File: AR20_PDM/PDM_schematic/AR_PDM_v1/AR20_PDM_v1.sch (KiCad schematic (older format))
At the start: 21 parts, among them J1 S_T_?, J2 1-776163-1, U1 ACM_2020

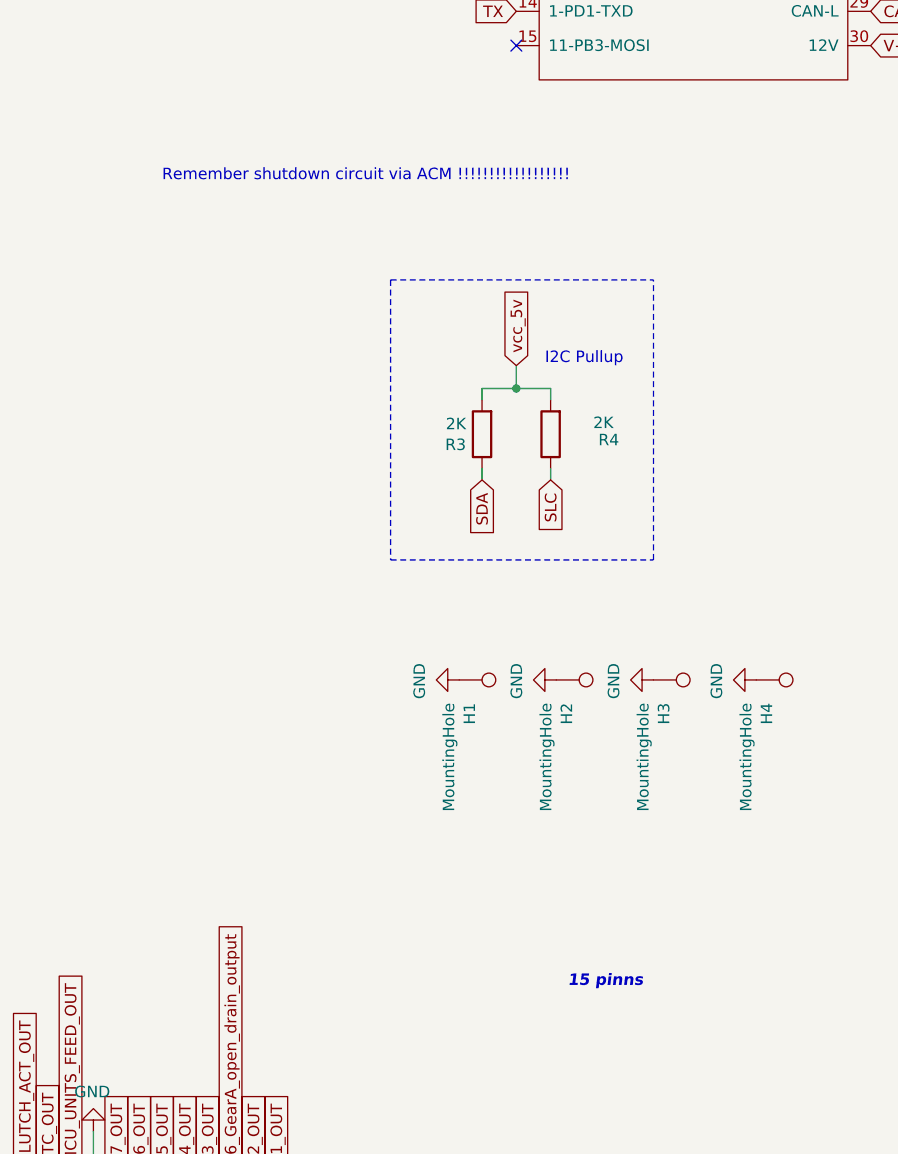
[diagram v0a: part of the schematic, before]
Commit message: Generated new gerberfile, with forgotten solder mask
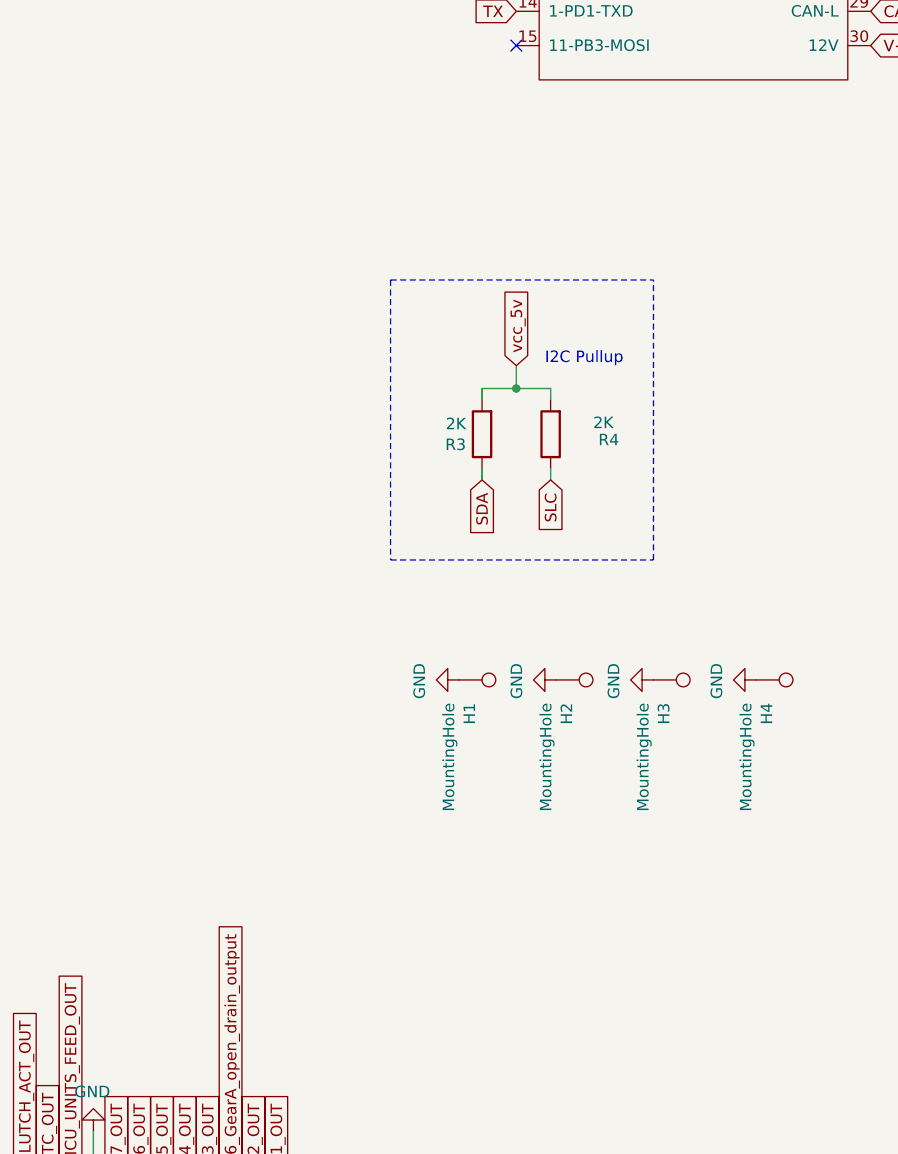
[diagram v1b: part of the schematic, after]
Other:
- note removed: "15 pinns"
- note removed: "Remember shutdown circuit via ACM !!!!!!!!!!!!!!!!!!"
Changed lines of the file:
@@
 Text GLabel 8775 7875 1    50   Input ~ 0
 SHUTDOWN_OUT
-Text Notes 13850 7050 0    50   Italic 10
-15 pinns
 Text Notes 13750 4325 0    50   ~ 0
 I2C Pullup
@@
 Wire Wire Line
 	2125 4475 2225 4475
-Text Notes 12075 3525 0    50   ~ 0
-Remember shutdown circuit via ACM !!!!!!!!!!!!!!!!!!
 Text GLabel 10100 1275 2    50   Input ~ 0
 ACM_Shutdown_Circuit

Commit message: Major redesign. schematics completed, PCB work in progress
-TODO : A proper changelog file. Where all changes will apear 
- Redesigned schematics to accommodate errors in the improvement list
- More detail in ALPHA improvement list
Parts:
- D1, D2, D3, D4: symbol AR20_PDM_v1-rescue:D_Zener-Device -> AR20_PDM_v1-rescue:D_Flyback-Zener
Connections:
- net labels added: Mux_enable, Mux_select_A0, Mux_select_A1, Shutdown_Relay_Side
- net labels removed: COIL_INJECTOR_Alert, FP_Alert, P1_MOS_SENSE_Select, P2_MOS_SENSE_Select, P3_MOS_SENSE_Select, P4_MOS_SENSE_Select, P5_MOS_SENSE_Select, P6_MOS_SENSE_Select, P7_MOS_SENSE_Select, Shutdown_Led
- no-connect marks 11 -> 13
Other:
- moved on the sheet: C1, C2, C3, C4, C5, C6, J1, J2, R1

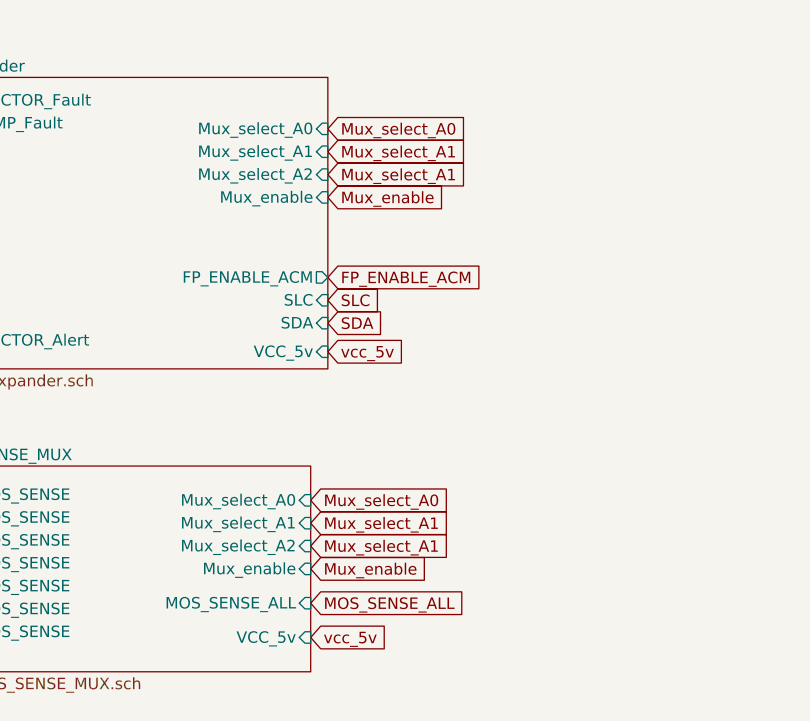
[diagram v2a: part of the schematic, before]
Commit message: All components in place - PCB work in progress
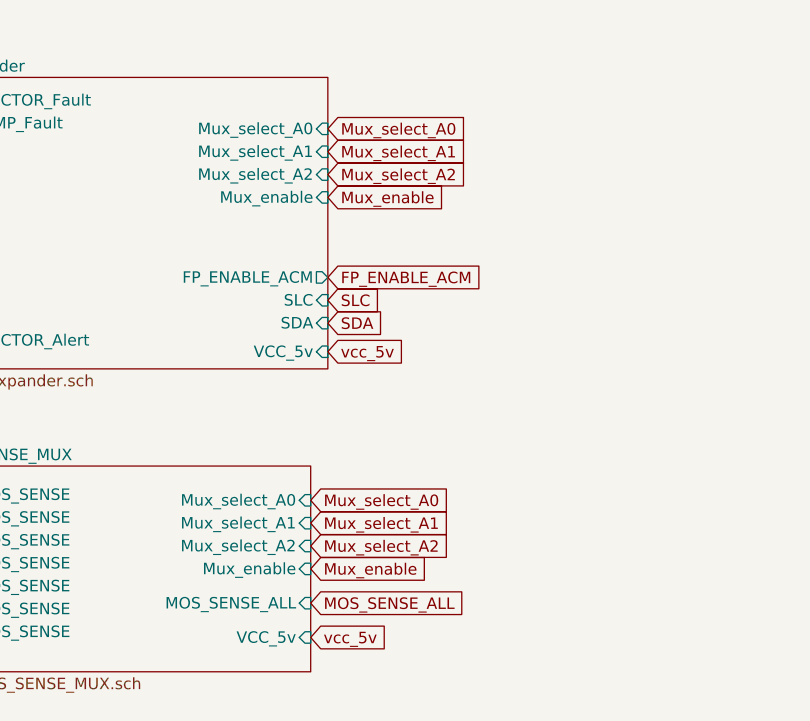
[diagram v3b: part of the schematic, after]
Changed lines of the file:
@@
 Mux_select_A1
 Text GLabel 10050 3400 2    50   Input ~ 0
-Mux_select_A1
+Mux_select_A2
 Text GLabel 9975 4825 2    50   Input ~ 0
 Mux_select_A0
@@
 Mux_select_A1
 Text GLabel 9975 5025 2    50   Input ~ 0
-Mux_select_A1
+Mux_select_A2
 Text GLabel 10050 3500 2    50   Input ~ 0
 Mux_enable

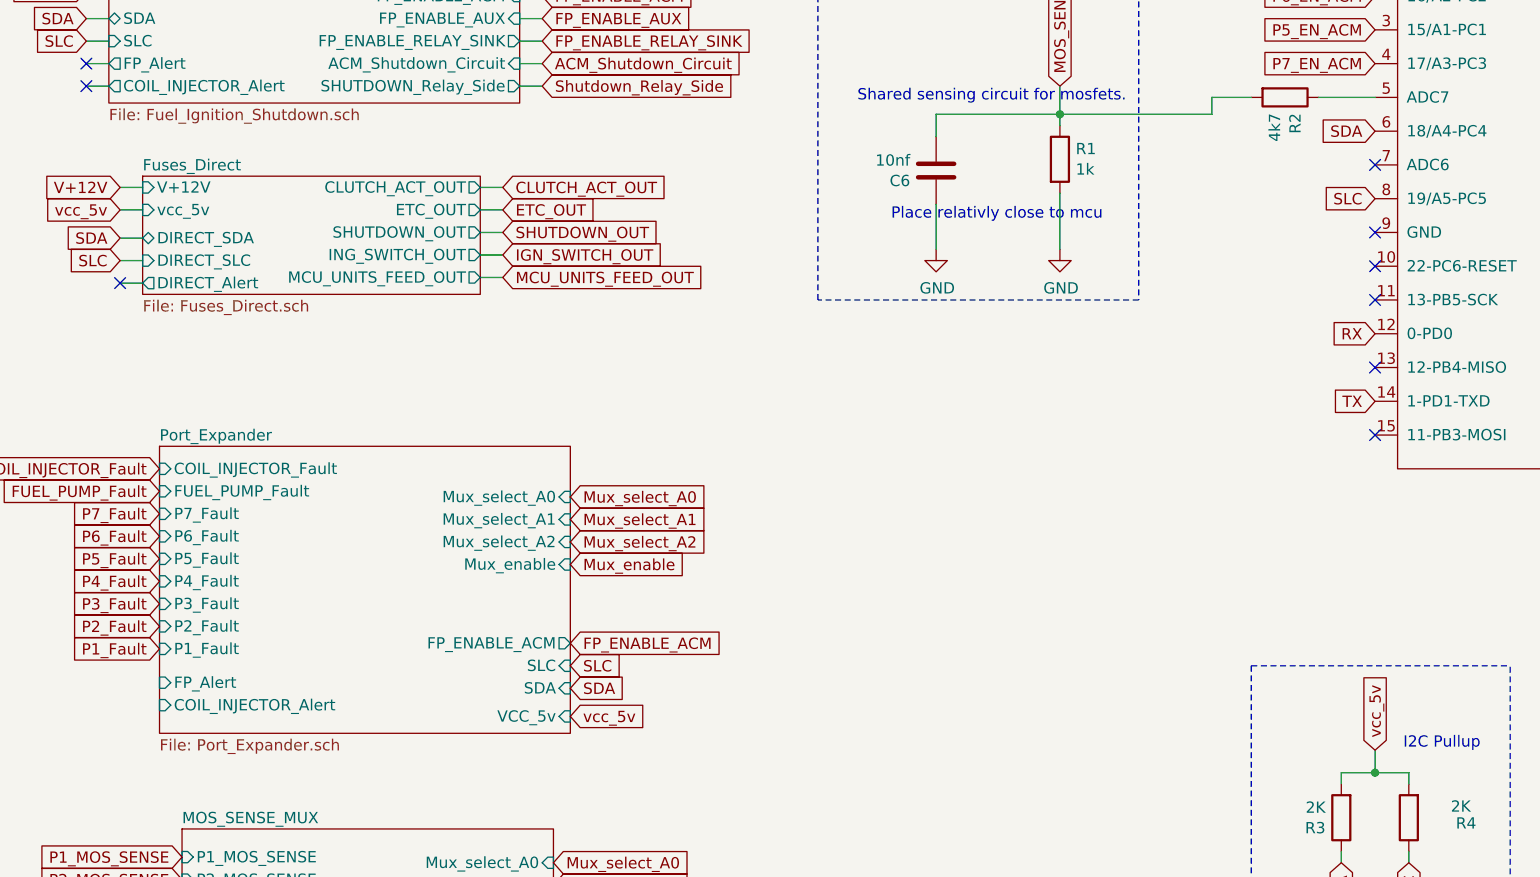
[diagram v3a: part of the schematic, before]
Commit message: End of Beta beginning of Charlie.
- RE0.2mm rework, jlc pcb minimum clearance with 2 OZ copper, was not advertised, properly
a retrace
Re positioning of some of components
added temp sensor
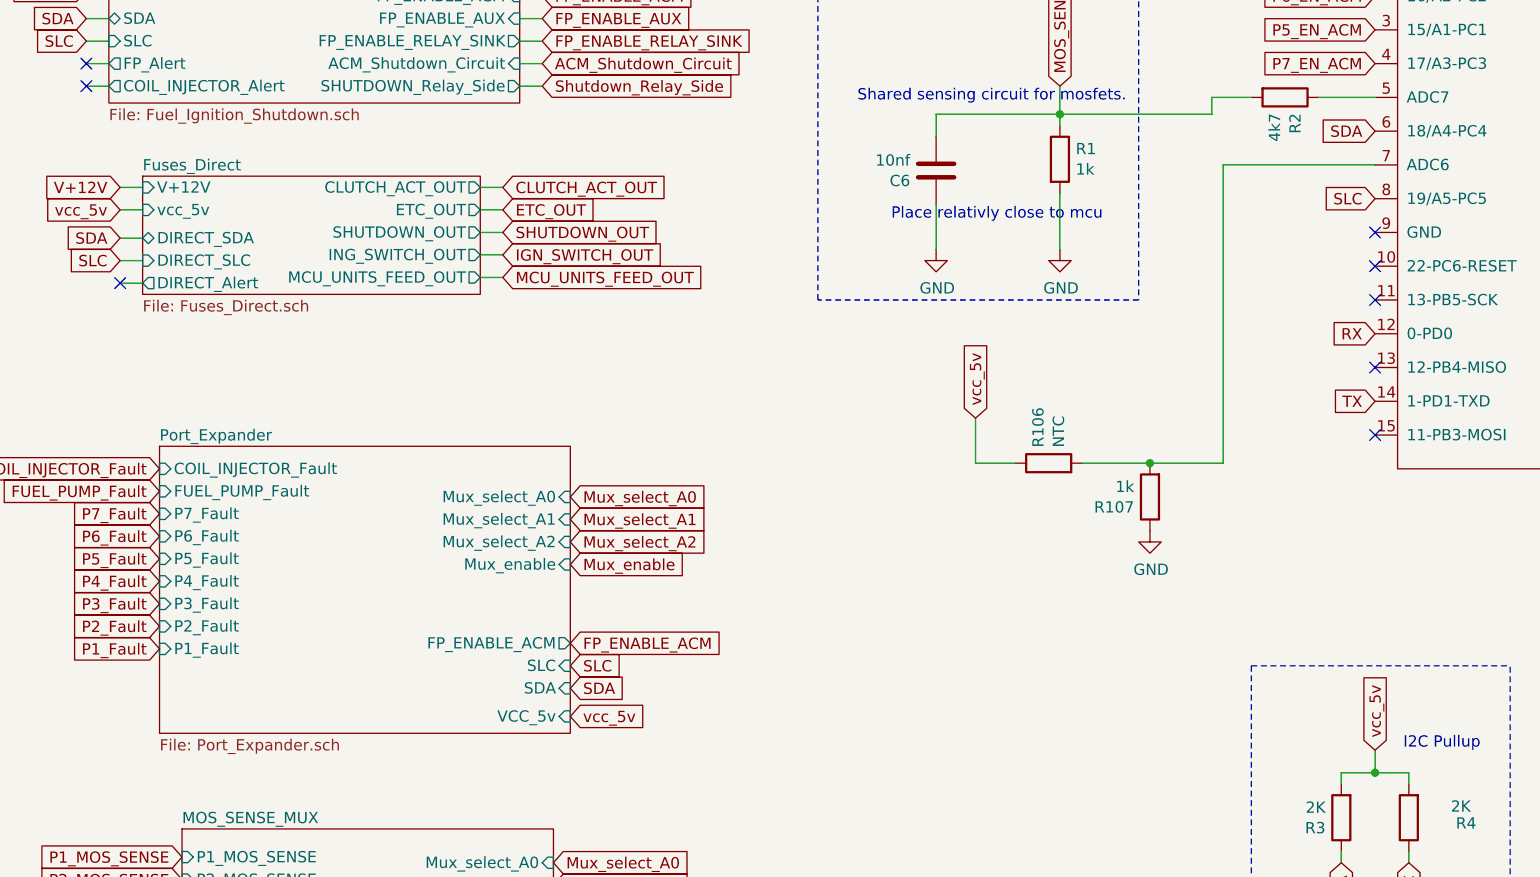
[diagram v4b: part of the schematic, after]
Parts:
- added R106: NTC, Resistor_SMD:R_0603_1608Metric, symbol AR20_PDM_v1-rescue:R-Device
- added R107: 1k, Resistor_SMD:R_0603_1608Metric, symbol AR20_PDM_v1-rescue:R-Device
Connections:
- net GND: now also R107.1
- net vcc_5v: now also R106.1
- net at U1.7 (ADC6): now also R106.2, R107.2
- no-connect marks 13 -> 12
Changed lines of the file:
@@
 EESchema Schematic File Version 4
-LIBS:AR20_PDM_v1-cache
 EELAYER 30 0
 EELAYER END
@@
 Text GLabel 13625 825  0    50   Input ~ 0
 ACM_Shutdown_Circuit
-NoConn ~ 13625 2325
 NoConn ~ 13625 2175
 NoConn ~ 13625 2625
@@
 Wire Wire Line
 	13375 1425 13625 1425
-NoConn ~ 13625 1725
 Text GLabel 15175 1725 2    50   Input ~ 0
 Switch
@@
 F12 "P2_Fault" I L 8225 3775 50
 F13 "P1_Fault" I L 8225 3875 50
-F14 "FP_Alert" I L 8225 4025 50
-F15 "COIL_INJECTOR_Alert" I L 8225 4125 50
-F16 "FP_ENABLE_ACM" O R 10050 3850 50
-F17 "Mux_select_A0" I R 10050 3200 50
-F18 "Mux_select_A1" I R 10050 3300 50
-F19 "Mux_select_A2" I R 10050 3400 50
-F20 "Mux_enable" I R 10050 3500 50
+F14 "FP_ENABLE_ACM" O R 10050 3850 50
+F15 "Mux_select_A0" I R 10050 3200 50
+F16 "Mux_select_A1" I R 10050 3300 50
+F17 "Mux_select_A2" I R 10050 3400 50
+F18 "Mux_enable" I R 10050 3500 50
 $EndSheet
 NoConn ~ 7900 1275
 NoConn ~ 7900 1375
+NoConn ~ 13625 2325
+Wire Wire Line
+	13625 1725 12950 1725
+Wire Wire Line
+	12950 1725 12950 3050
+Wire Wire Line
+	12950 3050 12625 3050
+$Comp
+L AR20_PDM_v1-rescue:R-Device R?
+U 1 1 5E8D3B0F
+P 12625 3200
+AR Path="/5DA89415/5E8D3B0F" Ref="R?"  Part="1"
+AR Path="/5DEB10A1/5E8D3B0F" Ref="R?"  Part="1"
+AR Path="/5DEB20EA/5E8D3B0F" Ref="R?"  Part="1"
+AR Path="/5E0E4725/5E8D3B0F" Ref="R?"  Part="1"
+AR Path="/5E0E4A93/5E8D3B0F" Ref="R?"  Part="1"
+AR Path="/5E0E4EB5/5E8D3B0F" Ref="R?"  Part="1"
+AR Path="/5E0E5304/5E8D3B0F" Ref="R?"  Part="1"
+AR Path="/5E0E594B/5E8D3B0F" Ref="R?"  Part="1"
+AR Path="/5E0E607C/5E8D3B0F" Ref="R?"  Part="1"
+AR Path="/5E0FB5C8/5E8D3B0F" Ref="R?"  Part="1"
+AR Path="/5E0FBBBD/5E8D3B0F" Ref="R?"  Part="1"
+AR Path="/5E0FC3A2/5E8D3B0F" Ref="R?"  Part="1"
+AR Path="/5E0FCFDC/5E8D3B0F" Ref="R?"  Part="1"
+AR Path="/5E0FDCCC/5E8D3B0F" Ref="R?"  Part="1"
+AR Path="/5E10174B/5E8D3B0F" Ref="R?"  Part="1"
+AR Path="/5E8D3B0F" Ref="R107"  Part="1"
+F 0 "R107" H 12695 3246 50  0000 L CNN
+F 1 "1k" H 12695 3155 50  0000 L CNN
+F 2 "Resistor_SMD:R_0603_1608Metric" V 12555 3200 50  0001 C CNN
+F 3 "~" H 12625 3200 50  0001 C CNN
+	1    12625 3200
+	-1   0    0    1
+$EndComp
+$Comp
+L AR20_PDM_v1-rescue:GND-power #PWR?
+U 1 1 5E8D890C
+P 12625 3350
+AR Path="/5DA89415/5E8D890C" Ref="#PWR?"  Part="1"
+AR Path="/5DEB10A1/5E8D890C" Ref="#PWR?"  Part="1"
+AR Path="/5DEB20EA/5E8D890C" Ref="#PWR?"  Part="1"
+AR Path="/5E0E4725/5E8D890C" Ref="#PWR?"  Part="1"
+AR Path="/5E0E4A93/5E8D890C" Ref="#PWR?"  Part="1"
+AR Path="/5E0E4EB5/5E8D890C" Ref="#PWR?"  Part="1"
+AR Path="/5E0E5304/5E8D890C" Ref="#PWR?"  Part="1"
+AR Path="/5E0E594B/5E8D890C" Ref="#PWR?"  Part="1"
+AR Path="/5E0E607C/5E8D890C" Ref="#PWR?"  Part="1"
+AR Path="/5E0FB5C8/5E8D890C" Ref="#PWR?"  Part="1"
+AR Path="/5E0FBBBD/5E8D890C" Ref="#PWR?"  Part="1"
+AR Path="/5E0FC3A2/5E8D890C" Ref="#PWR?"  Part="1"
+AR Path="/5E0FCFDC/5E8D890C" Ref="#PWR?"  Part="1"
+AR Path="/5E0FDCCC/5E8D890C" Ref="#PWR?"  Part="1"
+AR Path="/5E10174B/5E8D890C" Ref="#PWR?"  Part="1"
+AR Path="/5E8D890C" Ref="#PWR0166"  Part="1"
+F 0 "#PWR0166" H 12625 3100 50  0001 C CNN
+F 1 "GND" H 12630 3177 50  0000 C CNN
+F 2 "" H 12625 3350 50  0001 C CNN
+F 3 "" H 12625 3350 50  0001 C CNN
+	1    12625 3350
+	1    0    0    -1
+$EndComp
+Connection ~ 12625 3050
+$Comp
+L AR20_PDM_v1-rescue:R-Device R?
+U 1 1 5E8AD5D3
+P 12175 3050
+AR Path="/5DA89415/5E8AD5D3" Ref="R?"  Part="1"
+AR Path="/5DEB10A1/5E8AD5D3" Ref="R?"  Part="1"
+AR Path="/5DEB20EA/5E8AD5D3" Ref="R?"  Part="1"
+AR Path="/5E0E4725/5E8AD5D3" Ref="R?"  Part="1"
+AR Path="/5E0E4A93/5E8AD5D3" Ref="R?"  Part="1"
+AR Path="/5E0E4EB5/5E8AD5D3" Ref="R?"  Part="1"
+AR Path="/5E0E5304/5E8AD5D3" Ref="R?"  Part="1"
+AR Path="/5E0E594B/5E8AD5D3" Ref="R?"  Part="1"
+AR Path="/5E0E607C/5E8AD5D3" Ref="R?"  Part="1"
+AR Path="/5E0FB5C8/5E8AD5D3" Ref="R?"  Part="1"
+AR Path="/5E0FBBBD/5E8AD5D3" Ref="R?"  Part="1"
+AR Path="/5E0FC3A2/5E8AD5D3" Ref="R?"  Part="1"
+AR Path="/5E0FCFDC/5E8AD5D3" Ref="R?"  Part="1"
+AR Path="/5E0FDCCC/5E8AD5D3" Ref="R?"  Part="1"
+AR Path="/5E10174B/5E8AD5D3" Ref="R?"  Part="1"
+AR Path="/5E8AD5D3" Ref="R106"  Part="1"
+F 0 "R106" H 12245 3096 50  0000 L CNN
+F 1 "NTC" H 12245 3005 50  0000 L CNN
+F 2 "Resistor_SMD:R_0603_1608Metric" V 12105 3050 50  0001 C CNN
+F 3 "~" H 12175 3050 50  0001 C CNN
+	1    12175 3050
+	0    -1   -1   0
+$EndComp
+Wire Wire Line
+	12325 3050 12625 3050
+Wire Wire Line
+	12025 3050 11850 3050
+Wire Wire Line
+	11850 2850 11850 3050
+Text GLabel 11850 2850 1    50   Input ~ 0
+vcc_5v
 $EndSCHEMATC
